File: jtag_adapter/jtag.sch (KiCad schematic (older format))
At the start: 26 parts, among them J2 Conn_ARM_JTAG_SWD_20, Q1 BSS138, Q2 BSS138, U4 SN74AXCH4T245PW, U5 SN74AXCH4T245PW, U6 SN74AXCH1T45DBVR

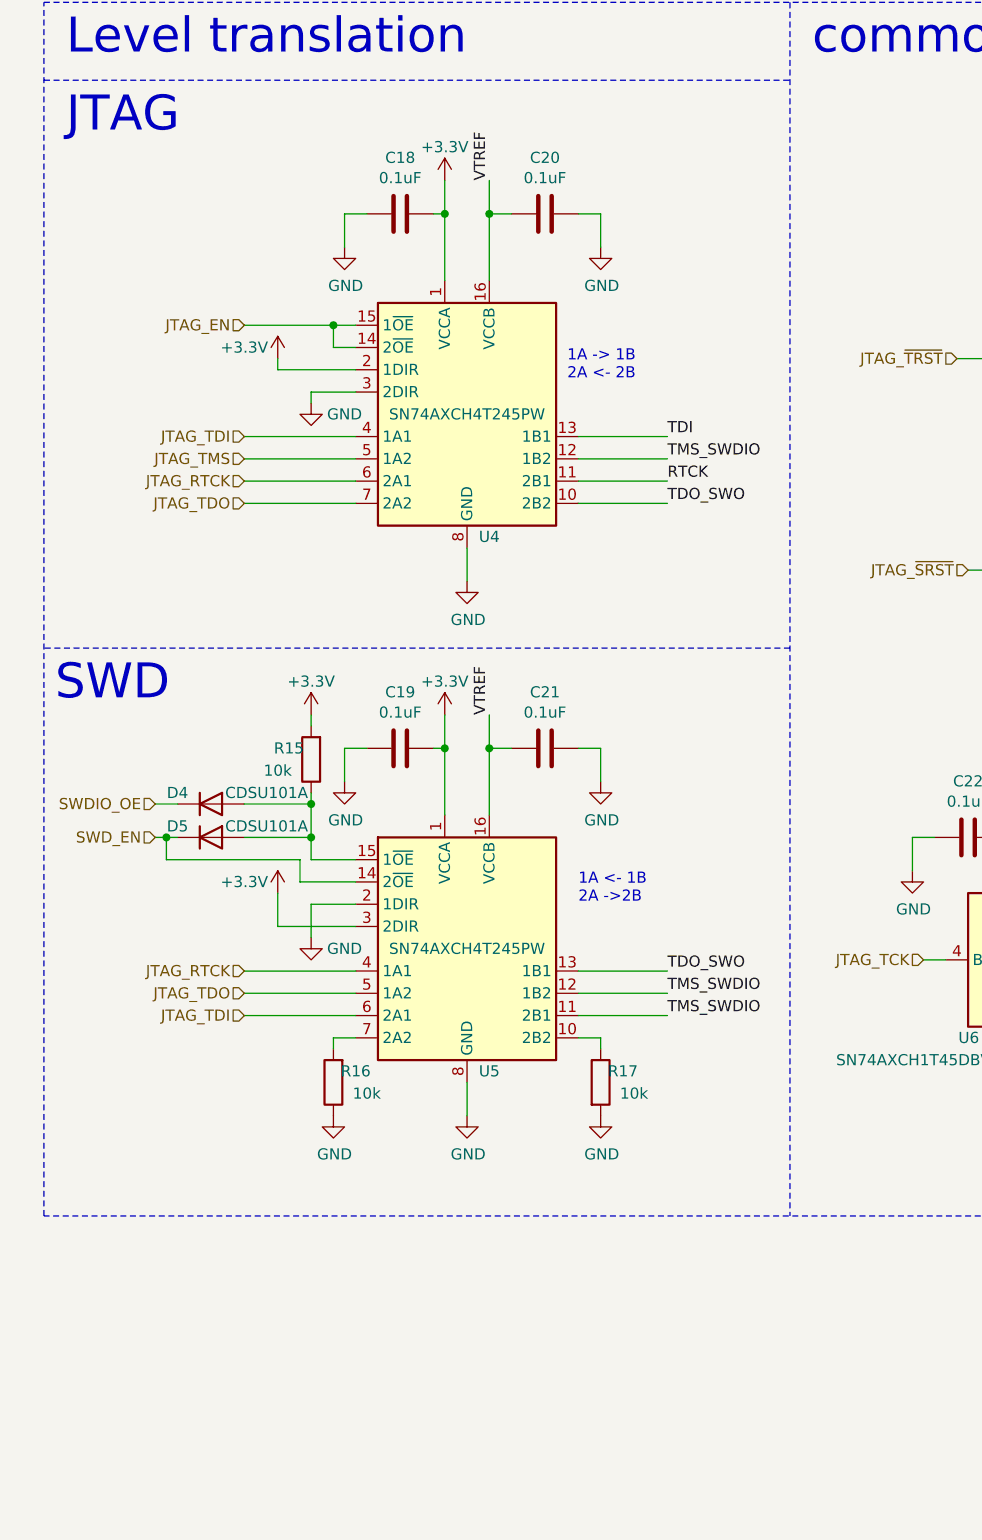
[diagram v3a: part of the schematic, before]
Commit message: wip: remove JTAG_EN pin
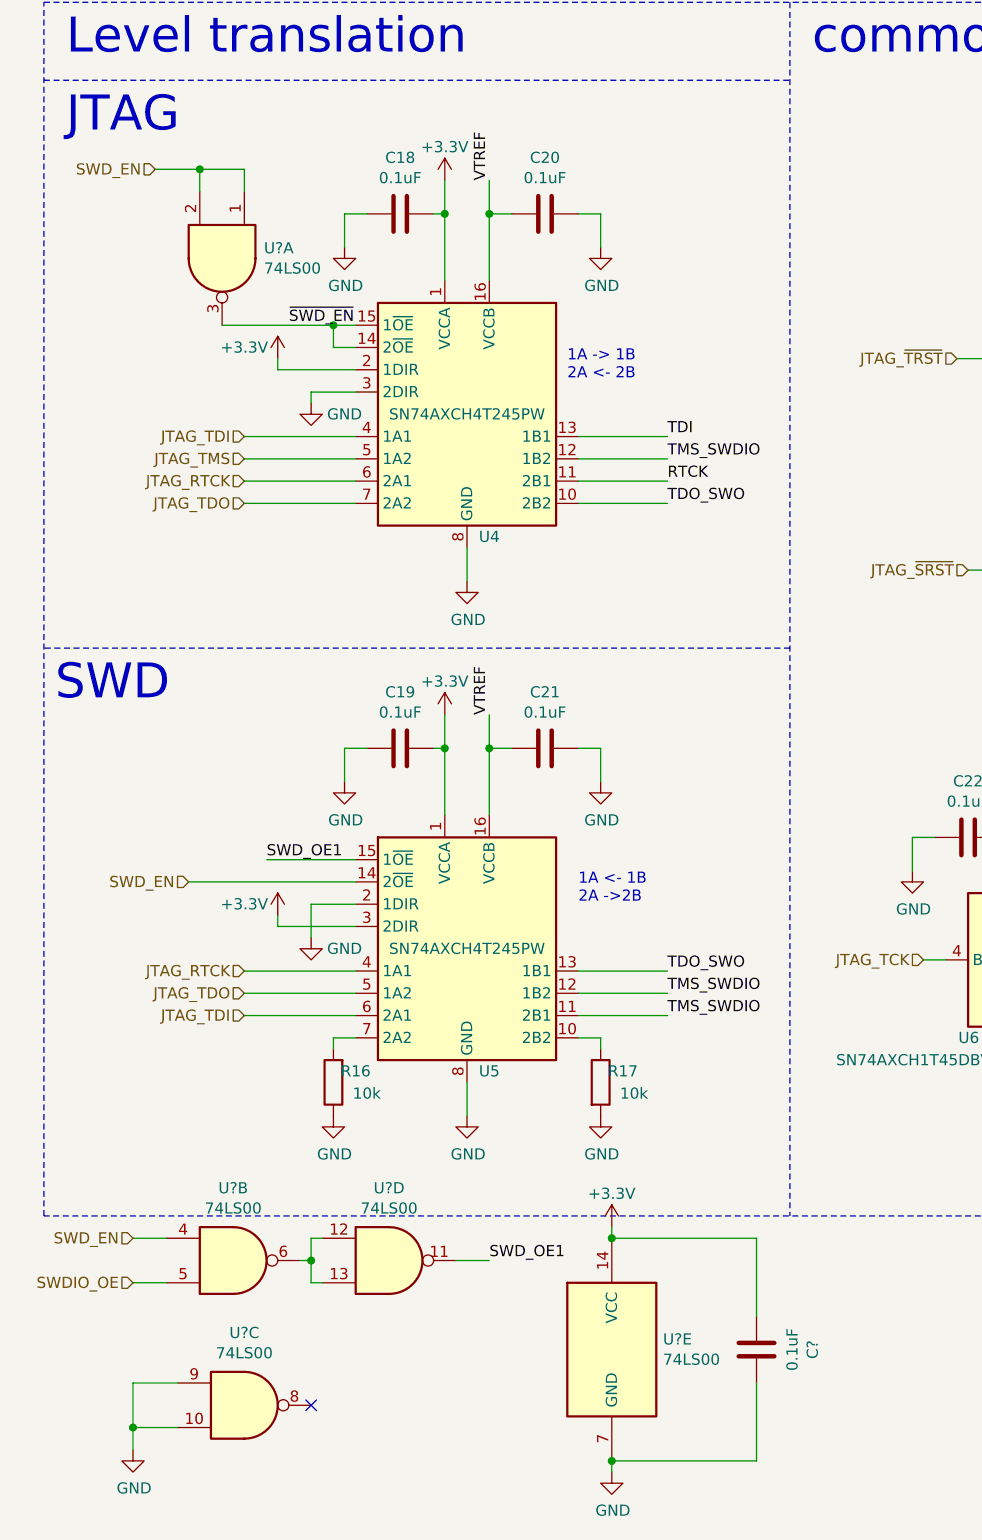
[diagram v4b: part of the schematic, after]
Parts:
- removed D4, D5: CDSU101A, Diode_SMD:D_SOD-523, symbol Device:D
- removed R15: 10k, Resistor_SMD:R_0603_1608Metric, symbol Device:R
- added C?: 0.1uF, Capacitor_SMD:C_0603_1608Metric, symbol Device:C
- added U? (x5): 74LS00, symbol 74xx:74LS00
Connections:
- net +3V3: now also C?.2, U?.14 (VCC)
- net GND: now also C?.1, U?.10, U?.7 (GND), U?.9
- net SWDIO_OE: now also U?.5
- net SWD_EN: now also U?.1, U?.2, U?.4
- net SWD_OE1: now reaches U5.15 (1~OE)
- net SWD_OE1: now also U?.11
- net JTAG_EN renamed ~SWD_EN
- net ~SWD_EN: now also U?.3
- new net: U?.12, U?.13, U?.6
- no-connect marks 3 -> 4
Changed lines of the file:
@@
 	1    0    0    -1
 $EndComp
-Text HLabel 1250 4600 0    50   Input ~ 0
-SWDIO_OE
 Text HLabel 1650 3250 0    50   Input ~ 0
 JTAG_TDO
@@
 	1    0    0    -1
 $EndComp
-Text HLabel 1650 2450 0    50   Input ~ 0
-JTAG_EN
 Wire Wire Line
 	2550 1950 2550 2250
@@
 Wire Wire Line
 	2050 2550 2150 2550
-Connection ~ 2050 2450
 $Comp
 L power:GND #PWR054
@@
 Wire Wire Line
 	1650 3250 2150 3250
-Wire Wire Line
-	1650 2450 2050 2450
 Text Label 7250 3550 0    50   ~ 0
 TMS_SWDIO
@@
 L power:+3.3V #PWR055
 U 1 1 612EF423
-P 1800 5000
-F 0 "#PWR055" H 1800 4850 50  0001 C CNN
-F 1 "+3.3V" H 1650 5050 50  0000 C CNN
-F 2 "" H 1800 5000 50  0001 C CNN
-F 3 "" H 1800 5000 50  0001 C CNN
-	1    1800 5000
+P 1800 5100
+F 0 "#PWR055" H 1800 4950 50  0001 C CNN
+F 1 "+3.3V" H 1650 5150 50  0000 C CNN
+F 2 "" H 1800 5100 50  0001 C CNN
+F 3 "" H 1800 5100 50  0001 C CNN
+	1    1800 5100
 	1    0    0    -1
 $EndComp
@@
 Text HLabel 1650 5550 0    50   Input ~ 0
 JTAG_TDI
-Wire Wire Line
-	1900 4850 1900 4950
-Wire Wire Line
-	1900 4950 2150 4950
-Text HLabel 1250 4750 0    50   Input ~ 0
+Text HLabel 1400 4950 0    50   Input ~ 0
 SWD_EN
-$Comp
-L Device:D D4
-U 1 1 612FA2D5
-P 1500 4600
-F 0 "D4" H 1350 4650 50  0000 C CNN
-F 1 "CDSU101A" H 1750 4650 50  0000 C CNN
-F 2 "Diode_SMD:D_SOD-523" H 1500 4600 50  0001 C CNN
-F 3 "~" H 1500 4600 50  0001 C CNN
-	1    1500 4600
-	1    0    0    -1
-$EndComp
-$Comp
-L Device:D D5
-U 1 1 612FB806
-P 1500 4750
-F 0 "D5" H 1350 4800 50  0000 C CNN
-F 1 "CDSU101A" H 1750 4800 50  0000 C CNN
-F 2 "Diode_SMD:D_SOD-523" H 1500 4750 50  0001 C CNN
-F 3 "~" H 1500 4750 50  0001 C CNN
-	1    1500 4750
-	1    0    0    -1
-$EndComp
-Wire Wire Line
-	1650 4600 1950 4600
-Wire Wire Line
-	1950 4750 1950 4600
-Wire Wire Line
-	1650 4750 1950 4750
-Wire Wire Line
-	1250 4600 1350 4600
-Wire Wire Line
-	1350 4750 1300 4750
-Wire Wire Line
-	1950 4850 2150 4850
 $Comp
 L Device:R R?
@@
 	1    0    0    -1
 $EndComp
-$Comp
-L power:+3.3V #PWR057
-U 1 1 612FF5CD
-P 1950 4200
-F 0 "#PWR057" H 1950 4050 50  0001 C CNN
-F 1 "+3.3V" H 1950 4350 50  0000 C CNN
-F 2 "" H 1950 4200 50  0001 C CNN
-F 3 "" H 1950 4200 50  0001 C CNN
-	1    1950 4200
-	1    0    0    -1
-$EndComp
-$Comp
-L Device:R R?
-U 1 1 612FF8E0
-P 1950 4400
-AR Path="/612FF8E0" Ref="R?"  Part="1"
-AR Path="/613347ED/612FF8E0" Ref="R15"  Part="1"
-F 0 "R15" H 2050 4350 50  0000 C CNN
-F 1 "10k" H 2100 4450 50  0000 C CNN
-F 2 "Resistor_SMD:R_0603_1608Metric" V 1880 4400 50  0001 C CNN
-F 3 "~" H 1950 4400 50  0001 C CNN
-F 4 "" H 1950 4400 50  0001 C CNN "MPN"
-	1    1950 4400
-	-1   0    0    1
-$EndComp
-Wire Wire Line
-	1300 4750 1300 4850
-Wire Wire Line
-	1300 4850 1900 4850
-Connection ~ 1300 4750
-Wire Wire Line
-	1300 4750 1250 4750
-Wire Wire Line
-	1950 4750 1950 4850
-Connection ~ 1950 4750
-Wire Wire Line
-	1950 4200 1950 4250
-Wire Wire Line
-	1950 4550 1950 4600
-Connection ~ 1950 4600
 Wire Notes Line
 	750  1000 6250 1000
@@
 	2150 5150 1800 5150
 Wire Wire Line
-	1800 5150 1800 5000
-Wire Wire Line
 	2150 5050 1950 5050
 Wire Wire Line
@@
 Text Notes 3100 2700 0    50   ~ 0
 1A -> 1B\n2A <- 2B\n
+Text HLabel 1250 1750 0    50   Input ~ 0
+SWD_EN
+Text Label 1850 2450 0    50   ~ 0
+~SWD_EN
+$Comp
+L 74xx:74LS00 U?
+U 1 1 614FD585
+P 1550 2150
+F 0 "U?" V 1504 2338 50  0000 L CNN
+F 1 "74LS00" V 1595 2338 50  0000 L CNN
+F 2 "" H 1550 2150 50  0001 C CNN
+F 3 "http://www.ti.com/lit/gpn/sn74ls00" H 1550 2150 50  0001 C CNN
+	1    1550 2150
+	0    1    1    0
+$EndComp
+$Comp
+L 74xx:74LS00 U?
+U 2 1 615000D2
+P 1600 6650
+F 0 "U?" H 1600 6975 50  0000 C CNN
+F 1 "74LS00" H 1600 6884 50  0000 C CNN
+F 2 "" H 1600 6650 50  0001 C CNN
+F 3 "http://www.ti.com/lit/gpn/sn74ls00" H 1600 6650 50  0001 C CNN
+	2    1600 6650
+	1    0    0    -1
+$EndComp
+$Comp
+L 74xx:74LS00 U?
+U 3 1 6150200F
+P 1650 7300
+F 0 "U?" H 1650 7625 50  0000 C CNN
+F 1 "74LS00" H 1650 7534 50  0000 C CNN
+F 2 "" H 1650 7300 50  0001 C CNN
+F 3 "http://www.ti.com/lit/gpn/sn74ls00" H 1650 7300 50  0001 C CNN
+	3    1650 7300
+	1    0    0    -1
+$EndComp
+$Comp
+L 74xx:74LS00 U?
+U 4 1 61505188
+P 2300 6650
+F 0 "U?" H 2300 6975 50  0000 C CNN
+F 1 "74LS00" H 2300 6884 50  0000 C CNN
+F 2 "" H 2300 6650 50  0001 C CNN
+F 3 "http://www.ti.com/lit/gpn/sn74ls00" H 2300 6650 50  0001 C CNN
+	4    2300 6650
+	1    0    0    -1
+$EndComp
+Wire Wire Line
+	1650 1850 1650 1750
+Wire Wire Line
+	1650 1750 1450 1750
+Wire Wire Line
+	1450 1850 1450 1750
+Connection ~ 1450 1750
+Wire Wire Line
+	1450 1750 1250 1750
+Wire Wire Line
+	1550 2450 2050 2450
+Connection ~ 2050 2450
+Wire Wire Line
+	1800 5150 1800 5100
+Wire Wire Line
+	1400 4950 2150 4950
+Text HLabel 1150 6550 0    50   Input ~ 0
+SWD_EN
+Text HLabel 1150 6750 0    50   Input ~ 0
+SWDIO_OE
+Wire Wire Line
+	2000 6550 1950 6550
+Wire Wire Line
+	1950 6550 1950 6650
+Wire Wire Line
+	1950 6650 1900 6650
+Wire Wire Line
+	1950 6650 1950 6750
+Wire Wire Line
+	1950 6750 2000 6750
+Connection ~ 1950 6650
+Wire Wire Line
+	1300 6750 1150 6750
+Wire Wire Line
+	1150 6550 1300 6550
+Text Label 1750 4850 0    50   ~ 0
+SWD_OE1
+Wire Wire Line
+	2150 4850 1750 4850
+Text Label 2750 6650 0    50   ~ 0
+SWD_OE1
+Wire Wire Line
+	2600 6650 2750 6650
+$Comp
+L power:GND #PWR?
+U 1 1 61584E1F
+P 1150 7500
+F 0 "#PWR?" H 1150 7250 50  0001 C CNN
+F 1 "GND" H 1155 7327 50  0000 C CNN
+F 2 "" H 1150 7500 50  0001 C CNN
+F 3 "" H 1150 7500 50  0001 C CNN
+	1    1150 7500
+	1    0    0    -1
+$EndComp
+Wire Wire Line
+	1350 7200 1150 7200
+Wire Wire Line
+	1150 7200 1150 7400
+Wire Wire Line
+	1350 7400 1150 7400
+Connection ~ 1150 7400
+Wire Wire Line
+	1150 7400 1150 7500
+NoConn ~ 1950 7300
+$Comp
+L power:GND #PWR?
+U 1 1 61594238
+P 3300 7600
+F 0 "#PWR?" H 3300 7350 50  0001 C CNN
+F 1 "GND" H 3305 7427 50  0000 C CNN
+F 2 "" H 3300 7600 50  0001 C CNN
+F 3 "" H 3300 7600 50  0001 C CNN
+	1    3300 7600
+	1    0    0    -1
+$EndComp
+$Comp
+L power:+3.3V #PWR?
+U 1 1 61594B24
+P 3300 6500
+F 0 "#PWR?" H 3300 6350 50  0001 C CNN
+F 1 "+3.3V" H 3300 6650 50  0000 C CNN
+F 2 "" H 3300 6500 50  0001 C CNN
+F 3 "" H 3300 6500 50  0001 C CNN
+	1    3300 6500
+	1    0    0    -1
+$EndComp
+$Comp
+L Device:C C?
+U 1 1 615A45C7
+P 3950 7050
+F 0 "C?" V 3698 7050 50  0000 C CNN
+F 1 "0.1uF" V 3789 7050 50  0000 C CNN
+F 2 "Capacitor_SMD:C_0603_1608Metric" H 3988 6900 50  0001 C CNN
+F 3 "~" H 3950 7050 50  0001 C CNN
+	1    3950 7050
+	-1   0    0    1
+$EndComp
+$Comp
+L 74xx:74LS00 U?
+U 5 1 61506D2C
+P 3300 7050
+F 0 "U?" H 3530 7096 50  0000 L CNN
+F 1 "74LS00" H 3530 7005 50  0000 L CNN
+F 2 "" H 3300 7050 50  0001 C CNN
+F 3 "http://www.ti.com/lit/gpn/sn74ls00" H 3300 7050 50  0001 C CNN
+	5    3300 7050
+	1    0    0    -1
+$EndComp
+Wire Wire Line
+	3300 6500 3300 6550
+Wire Wire Line
+	3300 6550 3950 6550
+Wire Wire Line
+	3950 6550 3950 6900
+Connection ~ 3300 6550
+Wire Wire Line
+	3950 7200 3950 7550
+Wire Wire Line
+	3950 7550 3300 7550
+Wire Wire Line
+	3300 7550 3300 7600
+Connection ~ 3300 7550
 $EndSCHEMATC

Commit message: wip: stash
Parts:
- removed R16, R17: 10k, Resistor_SMD:R_0603_1608Metric, symbol Device:R
- removed U? (x5): 74LS00, symbol 74xx:74LS00
- added U7: SN74LVC2G00DCUT, Package_SO:VSSOP-8_2.3x2mm_P0.5mm, symbol 74xGxx:74LVC2G00
- gave numbers to parts that had none: 1
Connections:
- net SWD_OE1 is gone; now on net ~SWD_EN: U5.15 (1~OE)
- net +3V3: now also U7.8 (VCC), U7.8 (VCC)
- net GND: now also U7.4 (GND), U7.4 (GND)
- net SWDIO_OE: now also U7.2
- net SWD_EN: now also U4.14 (2~OE), U4.15 (1~OE), U7.1, U7.5, U7.6; no longer U5.14 (2~OE)
- net ~SWD_EN: now also U7.3; no longer U4.14 (2~OE), U4.15 (1~OE)
- new net ~SWD_OE: U5.14 (2~OE), U7.7
- no-connect marks 4 -> 5
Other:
- note added: "Enabled when SWD_EN = 1"
- note added: "Enabled when SWD_EN=0"
- moved on the sheet: C24
